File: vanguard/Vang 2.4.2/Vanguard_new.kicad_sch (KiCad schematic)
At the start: 88 parts, among them J1 USB_C_Receptacle_USB2.0_16P, J2 Micro_SD_Card_Det1, J3 Conn_02x03_Odd_Even, J4 Conn_01x03, J5 Conn_01x03, J6 Conn_01x03, J7 Conn_01x02_Pin, Q1 BSS138, Q2 BSS138, Q3 BSS138, Q4 BSS138, U1 TXB0104D, U10 AP2112K-3.3, U2 BNO055, U3 ATSAMD11D14A-M, U4 BMP390L, U5 BD1020HFV, U6 AT25DF641A-SH-T, U7 ATmega4809-A, U8 TPS82130SILR, U9 TPS61092, Y1 Crystal

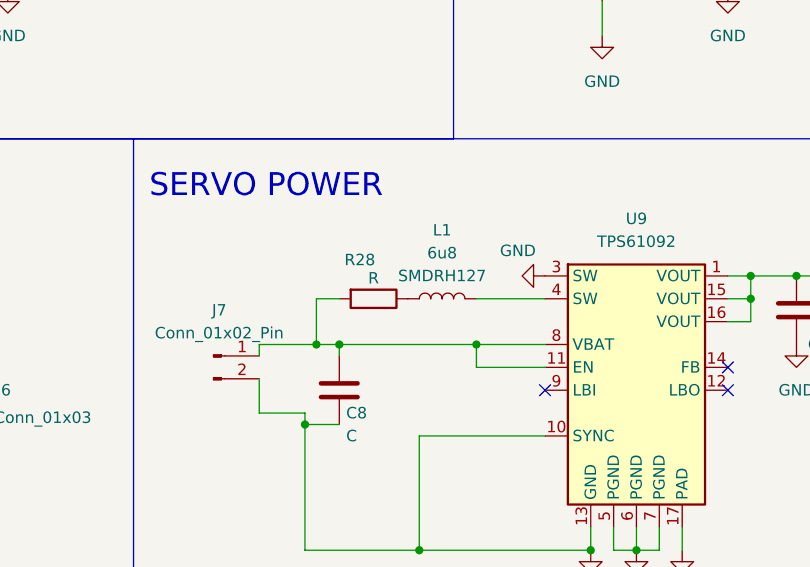
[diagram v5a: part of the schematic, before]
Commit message: SMDRI127-6R8NT symbol created and added to the library
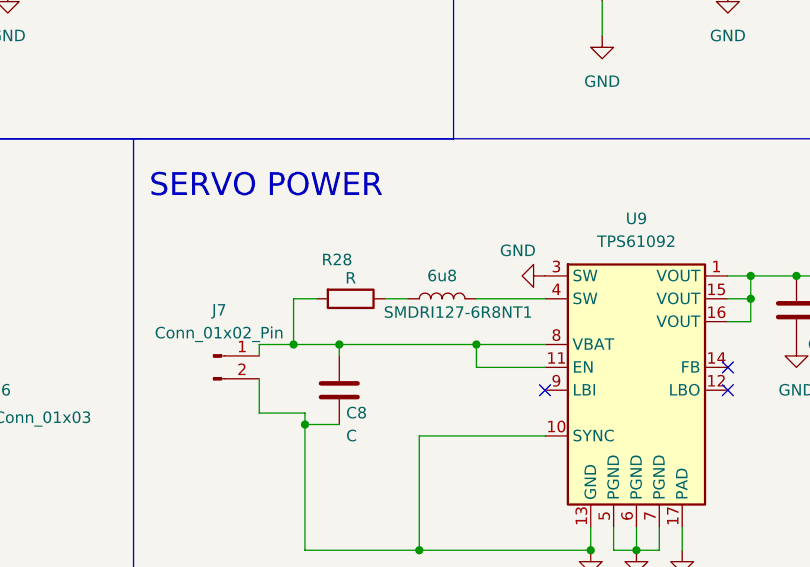
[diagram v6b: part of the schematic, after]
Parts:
- removed L1: 6u8, Inductor_SMD:L_0402_1005Metric, symbol Device:L
- added SMDRI127-6R8NT1: 6u8, symbol SMDRI127-6R8NT:L
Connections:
- net at U9.4 (SW): now also SMDRI127-6R8NT1.2
- net at R28.1: now also SMDRI127-6R8NT1.1
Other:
- moved on the sheet: R28
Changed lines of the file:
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@@
 	)
 	(junction
-		(at 345.44 162.56)
-		(diameter 0)
-		(color 0 0 0 0)
-	)
-	(junction
 		(at 162.56 60.96)
 		(diameter 0)
@@
 	)
 	(junction
+		(at 342.9 162.56)
+		(diameter 0)
+		(color 0 0 0 0)
+	)
+	(junction
 		(at 119.38 38.1)
 		(diameter 0)
@@
 	(wire
 		(pts
+			(xy 342.9 162.56) (xy 347.98 162.56)
+		)
+		(stroke
+			(width 0)
+			(type default)
+		)
+	)
+	(wire
+		(pts
 			(xy 386.08 185.42) (xy 386.08 182.88)
 		)
@@
 	(wire
 		(pts
-			(xy 345.44 162.56) (xy 347.98 162.56)
+			(xy 57.15 59.69) (xy 60.96 59.69)
 		)
 		(stroke
@@
 	(wire
 		(pts
-			(xy 57.15 59.69) (xy 60.96 59.69)
+			(xy 120.65 33.02) (xy 118.11 33.02)
 		)
 		(stroke
@@
 	(wire
 		(pts
-			(xy 120.65 33.02) (xy 118.11 33.02)
+			(xy 147.32 48.26) (xy 162.56 48.26)
 		)
 		(stroke
@@
 	(wire
 		(pts
-			(xy 147.32 48.26) (xy 162.56 48.26)
+			(xy 118.11 40.64) (xy 121.92 40.64)
 		)
 		(stroke
@@
 	(wire
 		(pts
-			(xy 118.11 40.64) (xy 121.92 40.64)
+			(xy 22.86 166.37) (xy 22.86 175.26)
 		)
 		(stroke
@@
 	(wire
 		(pts
-			(xy 22.86 166.37) (xy 22.86 175.26)
+			(xy 342.9 157.48) (xy 345.44 157.48)
 		)
 		(stroke
@@
 	(wire
 		(pts
-			(xy 345.44 157.48) (xy 347.98 157.48)
-		)
-		(stroke
-			(width 0)
-			(type default)
-		)
-	)
-	(wire
-		(pts
 			(xy 381 182.88) (xy 381 185.42)
 		)
@@
 	(wire
 		(pts
+			(xy 353.06 157.48) (xy 355.6 157.48)
+		)
+		(stroke
+			(width 0)
+			(type default)
+		)
+	)
+	(wire
+		(pts
 			(xy 383.54 185.42) (xy 383.54 182.88)
 		)
@@
 	(wire
 		(pts
-			(xy 345.44 157.48) (xy 345.44 162.56)
+			(xy 342.9 157.48) (xy 342.9 162.56)
 		)
 		(stroke
@@
 	(wire
 		(pts
-			(xy 339.09 162.56) (xy 345.44 162.56)
+			(xy 339.09 162.56) (xy 342.9 162.56)
 		)
 		(stroke
@@
 	(symbol
 		(lib_id "Device:R")
-		(at 351.79 157.48 270)
+		(at 349.25 157.48 270)
 		(unit 1)
 		(exclude_from_sim no)
@@
 		(dnp no)
 		(property "Reference" "R28"
-			(at 350.266 153.162 90)
+			(at 347.726 153.162 90)
 			(effects
 				(font
@@
 		)
 		(property "Value" "R"
-			(at 351.79 155.194 90)
+			(at 349.25 155.194 90)
 			(effects
 				(font
@@
 		)
 		(property "Footprint" "Resistor_SMD:R_0402_1005Metric"
-			(at 351.79 155.702 90)
+			(at 349.25 155.702 90)
 			(effects
 				(font
@@
 		)
 		(property "Datasheet" "~"
-			(at 351.79 157.48 0)
+			(at 349.25 157.48 0)
 			(effects
 				(font
@@
 		)
 		(property "Description" "Resistor"
-			(at 351.79 157.48 0)
+			(at 349.25 157.48 0)
 			(effects
 				(font
@@
 	)
 	(symbol
-		(lib_id "Device:L")
-		(at 359.41 157.48 90)
-		(unit 1)
-		(exclude_from_sim no)
-		(in_bom yes)
-		(on_board yes)
-		(dnp no)
-		(fields_autoplaced yes)
-		(property "Reference" "L1"
-			(at 359.41 149.86 90)
-			(effects
-				(font
-					(size 1.27 1.27)
-				)
-			)
-		)
-		(property "Value" "6u8"
-			(at 359.41 152.4 90)
-			(effects
-				(font
-					(size 1.27 1.27)
-				)
-			)
-		)
-		(property "Footprint" "Inductor_SMD:L_0402_1005Metric"
-			(at 359.41 157.48 0)
-			(effects
-				(font
-					(size 1.27 1.27)
-				)
-				(hide yes)
-			)
-		)
-		(property "Datasheet" "~"
-			(at 359.41 157.48 0)
-			(effects
-				(font
-					(size 1.27 1.27)
-				)
-				(hide yes)
-			)
-		)
-		(property "Description" "SMDRH127"
-			(at 359.41 154.94 90)
-			(effects
-				(font
-					(size 1.27 1.27)
-				)
-			)
-		)
-		(pin "2"
-		)
-		(pin "1"
-		)
-		(instances
-			(project ""
-				(path "/972fbf12-2dcd-4fdf-b1c9-8a2880c46640"
-					(reference "L1")
-					(unit 1)
-				)
-			)
-		)
-	)
-	(symbol
 		(lib_id "Transistor_FET:BSS138")
 		(at 214.63 55.88 270)
@@
 					(unit 1)
 				)
+			)
+		)
+	)
+	(symbol
+		(lib_id "SMDRI127-6R8NT:L")
+		(at 359.41 157.48 0)
+		(unit 1)
+		(exclude_from_sim no)
+		(in_bom yes)
+		(on_board yes)
+		(dnp no)
+		(property "Reference" "SMDRI127-6R8NT1"
+			(at 361.188 159.004 0)
+			(effects
+				(font
+					(size 1.27 1.27)
+				)
+			)
+		)
+		(property "Value" "6u8"
+			(at 359.41 154.94 0)
+			(effects
+				(font
+					(size 1.27 1.27)
+				)
+			)
+		)
+		(property "Footprint" ""
+			(at 359.41 157.48 90)
+			(effects
+				(font
+					(size 1.27 1.27)
+				)
+				(hide yes)
+			)
+		)
+		(property "Datasheet" "~"
+			(at 359.41 157.48 90)
+			(effects
+				(font
+					(size 1.27 1.27)
+				)
+				(hide yes)
+			)
+		)
+		(property "Description" "Inductor"
+			(at 359.156 161.29 0)
+			(effects
+				(font
+					(size 1.27 1.27)
+				)
+				(hide yes)
+			)
+		)
+		(pin "1"
+		)
+		(pin "2"
+		)
+		(instances
+			(project ""
+				(path "/972fbf12-2dcd-4fdf-b1c9-8a2880c46640"
+					(reference "SMDRI127-6R8NT1")
+					(unit 1)
+				)

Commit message: removed new comp and rename BD1020HFV to BD1020HFV-TR
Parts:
- removed LS1: CMI-1295-0585T, CMI-1295-0585T:CUI_CMI-1295-0585T, symbol CMI-1295-0585T[1]:CMI-1295-0585T
- removed SMDRI127-6R8NT1: 6u8, symbol SMDRI127-6R8NT:L
- removed U2: BNO055, Package_LGA:LGA-28_5.2x3.8mm_P0.5mm, symbol Sensor_Motion:BNO055
- removed U8: TPS82130SILR, TPS82130SILR:CONV_TPS82140SILR, symbol TPS82130SILR[1]:TPS82130SILR
- U5: value BD1020HFV -> BD1020HFV-TR
